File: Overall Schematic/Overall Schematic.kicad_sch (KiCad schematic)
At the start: 25 parts, among them U12 Spark MAX Motor Controller, U16 Spark MAX Motor Controller, U2 Jetson Nano, U20 Spark MAX Motor Controller, U24 Rev Neo, U25 Rev Neo, U26 Rev Neo, U27 Rev Neo, U28 E-STOP, U29 Power Distribution Panel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

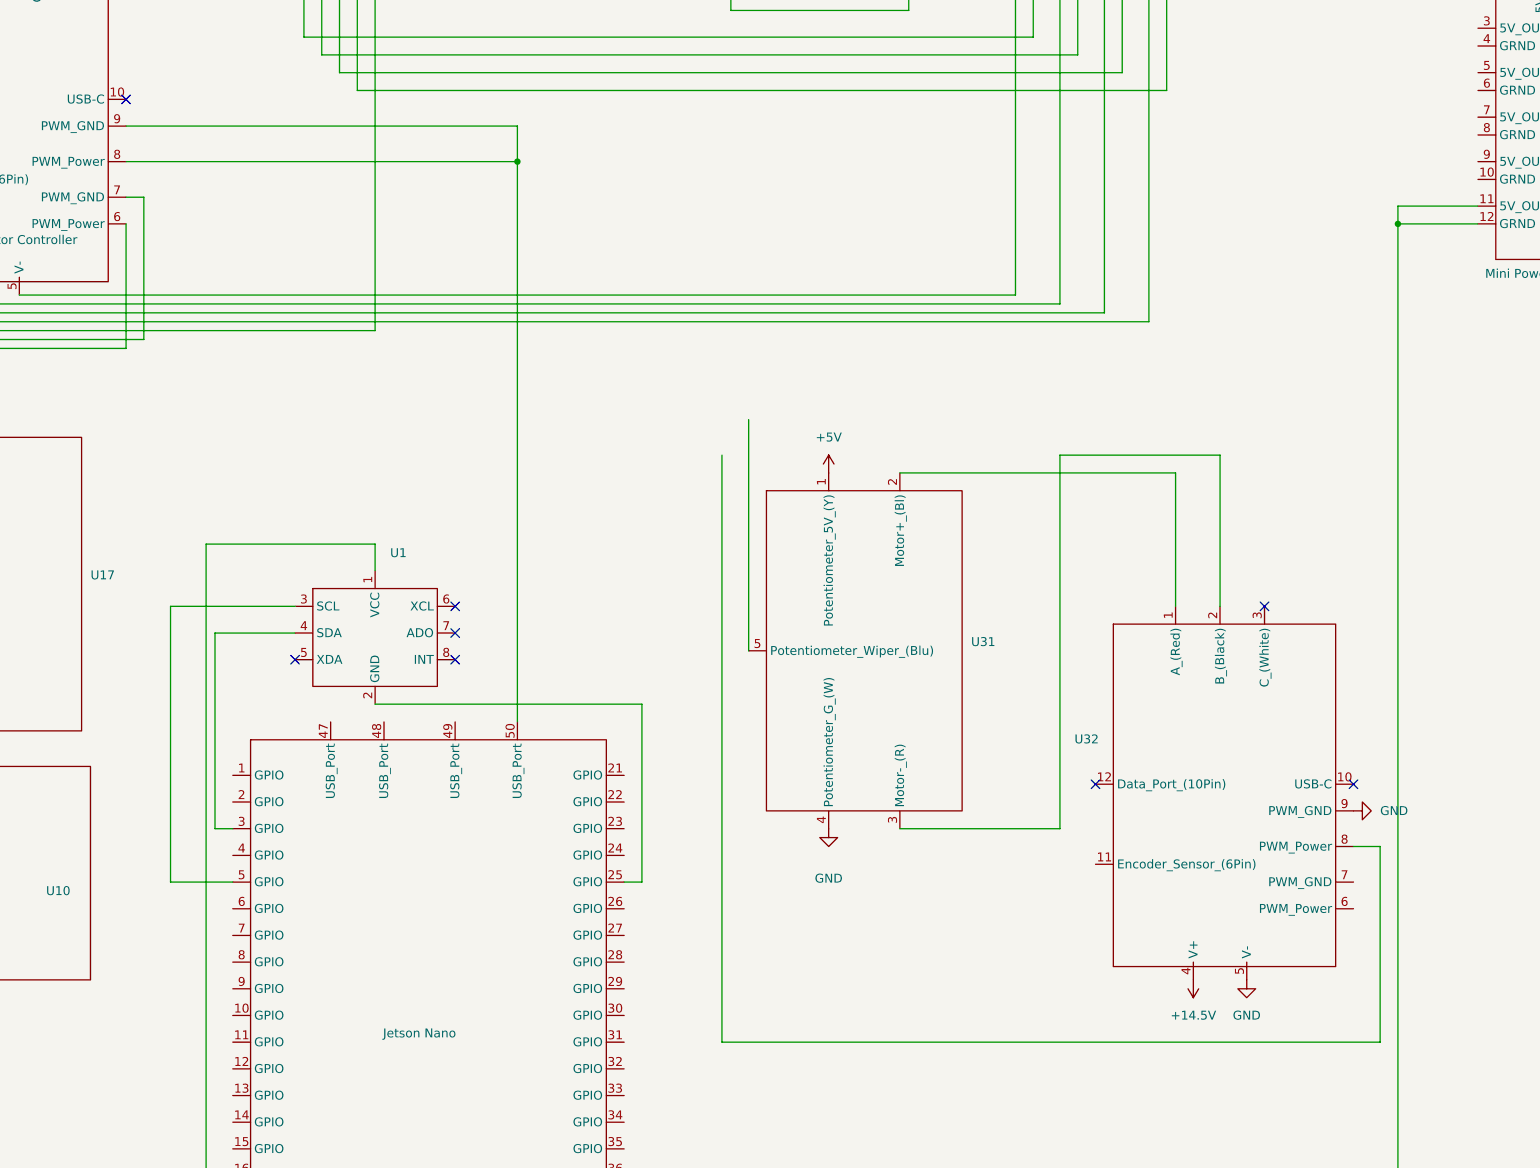
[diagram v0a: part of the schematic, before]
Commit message: Completed Update of Spark Max & Potentiometer Connections to Jetson Nano
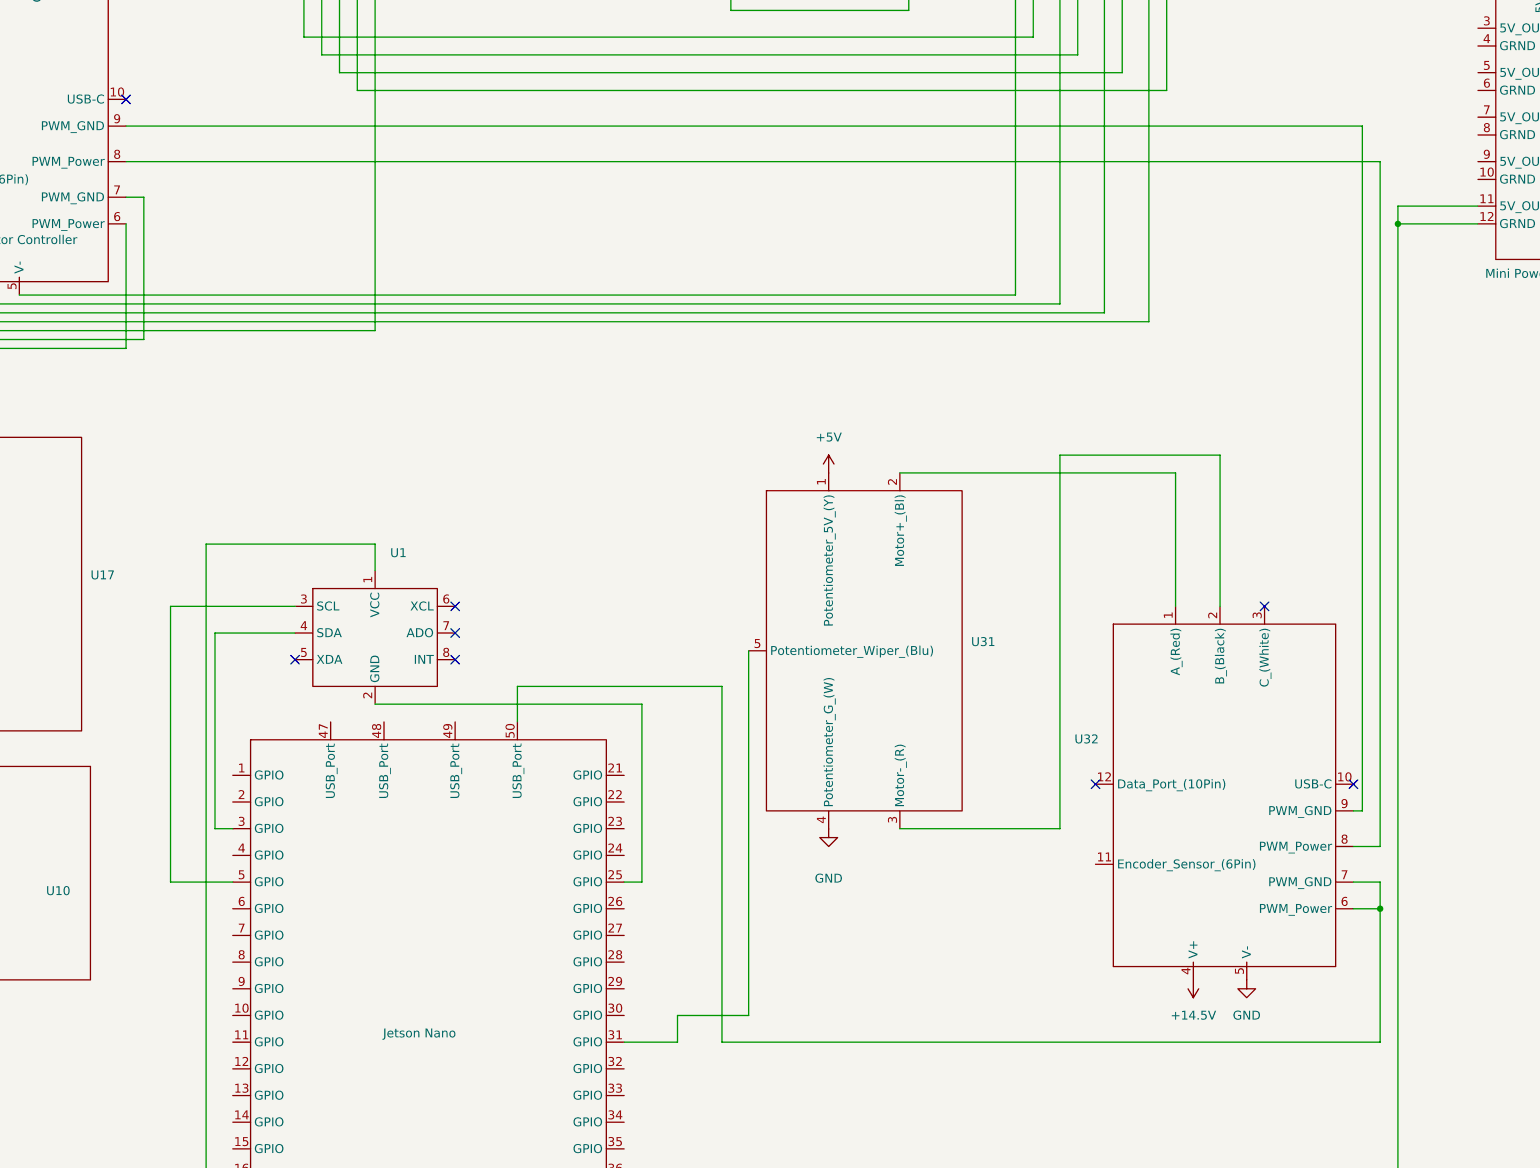
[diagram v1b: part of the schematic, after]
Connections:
- net GND: no longer U32.9 (PWM_GND)
- net at U32.6 (PWM_Power): now also U2.50 (USB_Port), U32.7 (PWM_GND)
- net at U32.8 (PWM_Power): now also U20.8 (PWM_Power)
- net at U31.5 (Potentiometer_Wiper_(Blu)): now also U2.31 (GPIO)
- net at U29. (GRND): no longer 14.8V-5V1. (5V_6A_OUT)
- new net: U20.9 (PWM_GND), U32.9 (PWM_GND)
- new net: 14.8V-5V1. (5V_6A_OUT), U29. (GRND)
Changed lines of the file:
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@@
 	)
 	(junction
-		(at 372.11 144.78)
+		(at 378.46 106.68)
 		(diameter 0)
 		(color 0 0 0 0)
 	)
 	(junction
-		(at 378.46 106.68)
+		(at 495.3 251.46)
 		(diameter 0)
 		(color 0 0 0 0)
@@
 	(wire
 		(pts
-			(xy 372.11 139.7) (xy 372.11 144.78)
-		)
-		(stroke
-			(width 0)
-			(type default)
-		)
-	)
-	(wire
-		(pts
 			(xy 152.4 161.29) (xy 152.4 167.64)
 		)
@@
 	(wire
 		(pts
+			(xy 491.49 251.46) (xy 495.3 251.46)
+		)
+		(stroke
+			(width 0)
+			(type default)
+		)
+	)
+	(wire
+		(pts
 			(xy 402.59 123.19) (xy 427.99 123.19)
 		)
@@
 	(wire
 		(pts
+			(xy 495.3 247.65) (xy 495.3 251.46)
+		)
+		(stroke
+			(width 0)
+			(type default)
+		)
+	)
+	(wire
+		(pts
 			(xy 176.53 60.96) (xy 346.71 60.96)
 		)
@@
 	(wire
 		(pts
+			(xy 401.32 270.51) (xy 401.32 219.71)
+		)
+		(stroke
+			(width 0)
+			(type default)
+		)
+	)
+	(wire
+		(pts
 			(xy 386.08 91.44) (xy 379.73 91.44)
 		)
@@
 	(wire
 		(pts
-			(xy 316.23 139.7) (xy 372.11 139.7)
+			(xy 316.23 139.7) (xy 492.76 139.7)
 		)
 		(stroke
@@
 	(wire
 		(pts
-			(xy 372.11 144.78) (xy 372.11 224.79)
+			(xy 220.98 138.43) (xy 220.98 64.77)
 		)
 		(stroke
@@
 	(wire
 		(pts
-			(xy 220.98 138.43) (xy 220.98 64.77)
+			(xy 497.84 153.67) (xy 509.27 153.67)
 		)
 		(stroke
 			(width 0)
 			(type default)
+			(color 0 0 0 1)
 		)
 	)
 	(wire
 		(pts
-			(xy 497.84 153.67) (xy 509.27 153.67)
+			(xy 379.73 63.5) (xy 375.92 63.5)
 		)
 		(stroke
@@
 	(wire
 		(pts
-			(xy 379.73 63.5) (xy 375.92 63.5)
+			(xy 349.25 58.42) (xy 349.25 134.62)
 		)
 		(stroke
 			(width 0)
 			(type default)
-			(color 0 0 0 1)
+			(color 255 0 0 1)
 		)
 	)
 	(wire
 		(pts
-			(xy 349.25 58.42) (xy 349.25 134.62)
+			(xy 492.76 237.49) (xy 492.76 139.7)
 		)
 		(stroke
 			(width 0)
 			(type default)
-			(color 255 0 0 1)
 		)
 	)
@@
 	(wire
 		(pts
-			(xy 405.13 181.61) (xy 405.13 214.63)
+			(xy 205.74 102.87) (xy 214.63 102.87)
 		)
 		(stroke
@@
 	(wire
 		(pts
-			(xy 205.74 102.87) (xy 214.63 102.87)
+			(xy 195.58 162.56) (xy 176.53 162.56)
 		)
 		(stroke
 			(width 0)
 			(type default)
+			(color 247 0 0 1)
 		)
 	)
 	(wire
 		(pts
-			(xy 195.58 162.56) (xy 176.53 162.56)
+			(xy 290.83 104.14) (xy 279.4 104.14)
 		)
 		(stroke
 			(width 0)
 			(type default)
-			(color 247 0 0 1)
 		)
 	)
 	(wire
 		(pts
-			(xy 290.83 104.14) (xy 279.4 104.14)
+			(xy 405.13 266.7) (xy 394.97 266.7)
 		)
 		(stroke
@@
 	(wire
 		(pts
+			(xy 387.35 270.51) (xy 394.97 270.51)
+		)
+		(stroke
+			(width 0)
+			(type default)
+		)
+	)
+	(wire
+		(pts
 			(xy 95.25 92.71) (xy 95.25 106.68)
 		)
@@
 	(wire
 		(pts
+			(xy 491.49 247.65) (xy 495.3 247.65)
+		)
+		(stroke
+			(width 0)
+			(type default)
+		)
+	)
+	(wire
+		(pts
 			(xy 77.47 64.77) (xy 95.25 64.77)
 		)
@@
 	(wire
 		(pts
+			(xy 495.3 144.78) (xy 495.3 242.57)
+		)
+		(stroke
+			(width 0)
+			(type default)
+		)
+	)
+	(wire
+		(pts
 			(xy 121.92 140.97) (xy 121.92 62.23)
 		)
@@
 	(wire
 		(pts
+			(xy 495.3 251.46) (xy 495.3 270.51)
+		)
+		(stroke
+			(width 0)
+			(type default)
+		)
+	)
+	(wire
+		(pts
 			(xy 445.77 127) (xy 445.77 113.03)
 		)
@@
 	(wire
 		(pts
+			(xy 495.3 242.57) (xy 491.49 242.57)
+		)
+		(stroke
+			(width 0)
+			(type default)
+		)
+	)
+	(wire
+		(pts
 			(xy 416.56 91.44) (xy 427.99 91.44)
 		)
@@
 	(wire
 		(pts
-			(xy 495.3 242.57) (xy 491.49 242.57)
-		)
-		(stroke
-			(width 0)
-			(type default)
-		)
-	)
-	(wire
-		(pts
 			(xy 327.66 199.39) (xy 327.66 293.37)
 		)
@@
 	(wire
 		(pts
-			(xy 401.32 186.69) (xy 401.32 270.51)
+			(xy 303.53 104.14) (xy 312.42 104.14)
 		)
 		(stroke
@@
 	(wire
 		(pts
-			(xy 303.53 104.14) (xy 312.42 104.14)
+			(xy 405.13 214.63) (xy 405.13 266.7)
 		)
 		(stroke
@@
 	(wire
 		(pts
+			(xy 394.97 266.7) (xy 394.97 270.51)
+		)
+		(stroke
+			(width 0)
+			(type default)
+		)
+	)
+	(wire
+		(pts
 			(xy 378.46 81.28) (xy 378.46 91.44)
 		)
@@
 	(wire
 		(pts
+			(xy 372.11 219.71) (xy 372.11 224.79)
+		)
+		(stroke
+			(width 0)
+			(type default)
+		)
+	)
+	(wire
+		(pts
 			(xy 255.27 104.14) (xy 264.16 104.14)
 		)
@@
 	(wire
 		(pts
-			(xy 495.3 270.51) (xy 495.3 242.57)
-		)
-		(stroke
-			(width 0)
-			(type default)
-		)
-	)
-	(wire
-		(pts
 			(xy 101.6 106.68) (xy 101.6 100.33)
 		)
@@
 	(wire
 		(pts
-			(xy 316.23 144.78) (xy 372.11 144.78)
+			(xy 491.49 237.49) (xy 492.76 237.49)
+		)
+		(stroke
+			(width 0)
+			(type default)
+		)
+	)
+	(wire
+		(pts
+			(xy 316.23 144.78) (xy 495.3 144.78)
 		)
 		(stroke
@@
 	(wire
 		(pts
+			(xy 401.32 219.71) (xy 372.11 219.71)
+		)
+		(stroke
+			(width 0)
+			(type default)
+		)
+	)
+	(wire
+		(pts
 			(xy 297.18 96.52) (xy 297.18 110.49)
 		)
@@
 					(unit 1)
 				)
-			)
-		)
-	)
-	(symbol
-		(lib_id "power:GND")
-		(at 491.49 237.49 90)
-		(unit 1)
-		(exclude_from_sim no)
-		(in_bom yes)
-		(on_board yes)
-		(dnp no)
-		(fields_autoplaced yes)
-		(property "Reference" "#PWR016"
-			(at 497.84 237.49 0)
-			(effects
-				(font
-					(size 1.27 1.27)
-				)
-				(hide yes)
-			)
-		)
-		(property "Value" "GND"
-			(at 495.3 237.4899 90)
-			(effects
-				(font
-					(size 1.27 1.27)
-				)
-				(justify right)
-			)
-		)
-		(property "Footprint" ""
-			(at 491.49 237.49 0)
-			(effects
-				(font
-					(size 1.27 1.27)
-				)
-				(hide yes)
-			)
-		)
-		(property "Datasheet" ""
-			(at 491.49 237.49 0)
-			(effects
-				(font
-					(size 1.27 1.27)
-				)
-				(hide yes)
-			)
-		)
-		(property "Description" "Power symbol creates a global label with name \"GND\" , ground"
-			(at 491.49 237.49 0)
-			(effects
-				(font
-					(size 1.27 1.27)
-				)
-				(hide yes)
-			)
-		)
-		(pin "1"
-		)
-		(instances
-			(project "Overall Schematic"
-				(path "/b876505b-23a1-4d11-8fd1-5d37220464c6"
-					(reference "#PWR016")
-					(unit 1)
-				)
